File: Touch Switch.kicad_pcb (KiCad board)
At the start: 2 copper layers, 39 parts, among them J1 Conn_01x03_Pin, J2 Conn_02x04_Counter_Clockwise, K1 Relay_SPST-NO, K2 Relay_SPST-NO, K3 Relay_SPST-NO, K4 Relay_SPST-NO, Q1 MMBT3904, Q2 MMBT3904, Q3 MMBT3904, Q5 MMBT3904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

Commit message: PCB V1
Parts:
- removed the R13 at (47.0, 65.4)
- removed the R13 at (47.0, 31.2)
- removed S7133S1: ~, Package_SO:SOP-8_3.9x4.9mm_P1.27mm
- added C1: 2,2µF - 400V, Capacitor_THT:CP_Radial_D8.0mm_P3.50mm, F.Cu at (171.2, 98.8)
- added C2: 470µF - 10V, Capacitor_THT:CP_Radial_D6.3mm_P2.50mm, F.Cu at (190.8, 76.5)
- added C3: 330µF - 10V, Capacitor_THT:CP_Radial_D6.3mm_P2.50mm, F.Cu at (172.8, 71.1)
- added C4: 100nF - 10V, Capacitor_SMD:C_0805_2012Metric, F.Cu at (179.3, 66.1)
- added C5: 100pF - 400V, footprint:PFR5101J400J11L4BULK, F.Cu at (172.5, 106.0)
- added J3: Conn_01x01_Pin, Connector_PinHeader_2.54mm:PinHeader_1x01_P2.54mm_Vertical, F.Cu at (235.7, 92.4)
- added J4: Conn_01x01_Pin, Connector_PinHeader_2.54mm:PinHeader_1x01_P2.54mm_Vertical, F.Cu at (235.7, 79.1)
- added J5: Conn_01x01_Pin, Connector_PinHeader_2.54mm:PinHeader_1x01_P2.54mm_Vertical, F.Cu at (235.7, 105.6)
- added J6: Conn_01x01_Pin, Connector_PinHeader_2.54mm:PinHeader_1x01_P2.54mm_Vertical, F.Cu at (235.7, 65.9)
- added R11: 10K, Resistor_SMD:R_0805_2012Metric, F.Cu at (203.6, 92.2)
- added R13: 10K, Resistor_SMD:R_0805_2012Metric, F.Cu at (203.8, 66.0)
- added S713XS1: ~, Package_SO:SOP-8_3.9x4.9mm_P1.27mm, F.Cu at (161.4, 87.1)
- added T1: Transformer_1P_2S, footprint:transformer, F.Cu at (183.9, 90.9)
- J1: footprint Diode_SMD:D_SMA -> Connector_PinHeader_2.54mm:PinHeader_1x03_P2.54mm_Vertical
- moved K1 198.1 mm to (220.6, 95.7), turned to 0 degrees
- moved K4 188.4 mm to (220.6, 82.4), turned to 0 degrees
- moved K2 186.7 mm to (220.6, 108.9), turned to 0 degrees
- moved K3 183.5 mm to (220.6, 69.2), turned to 0 degrees
- moved D5 179.2 mm to (208.1, 98.0), turned to 90 degrees
- moved Q5 172.9 mm to (204.6, 96.2), turned to 0 degrees
- moved D7 168.8 mm to (208.1, 85.0), turned to 90 degrees
- moved D6 167.0 mm to (208.1, 111.5), turned to 90 degrees
- moved D8 163.5 mm to (208.1, 71.6), turned to 90 degrees
- moved Q3 163.2 mm to (204.6, 83.2), turned to 0 degrees
- moved Q1 161.8 mm to (204.8, 109.7), turned to 0 degrees
- moved R14 159.4 mm to (203.6, 78.5), turned to 90 degrees
- moved Q2 158.9 mm to (204.6, 70.0), turned to 0 degrees
- moved R12 158.4 mm to (203.8, 105.7), turned to 90 degrees
- moved J2 134.4 mm to (193.0, 86.9), turned to 90 degrees
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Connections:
- F1 pad 1: L -> L1
- J1 pad 1: L -> L1
- Q1 pad 1: CT3 -> CT4
- Q2 pad 1: CT4 -> CT3
- Q3 pad 1: CT2 -> CT1
- Q5 pad 1: CT1 -> CT2
- R12 pad 1: CT3 -> CT4
- R14 pad 1: CT2 -> CT1
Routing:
- net +5V: track 0.00 -> 171.9 mm
- net +3.3V: track 0.00 -> 60.0 mm, vias 0 -> 1
- net 310VDC: track 0.00 -> 51.2 mm
- net L: track 0.00 -> 48.0 mm
- net Prim: track 0.00 -> 31.0 mm
- net CT4: track 0.00 -> 27.3 mm
- net CT3: track 0.00 -> 25.5 mm
- net VCC_IC: track 0.00 -> 25.1 mm, vias 0 -> 2
- net Net-(C7-Pad1): track 0.00 -> 23.1 mm
- net Net-(D1-+): track 0.00 -> 17.5 mm
- net Net-(S713XS1-FB): track 0.00 -> 17.0 mm
- net Sec: track 0.00 -> 15.8 mm
- net N: track 0.00 -> 15.3 mm
- net CT2: track 0.00 -> 14.7 mm
- net Net-(D7-A): track 0.00 -> 11.1 mm
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- added copper zone on B.Cu, net GND
- added copper zone on F.Cu, net GND
- added copper zone on B.Cu, net GND2
- added copper zone on F.Cu, net GND2
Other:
- board outline added: 95 x 54 mm
- board text added: "Touch-Switch Power-Card"

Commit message: PCB V2
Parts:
- R5, R6: footprint Resistor_SMD:R_1206_3216Metric -> Resistor_SMD:R_0805_2012Metric
- moved F1 19.1 mm to (156.8, 64.5), turned to 180 degrees
- moved R11 13.8 mm to (193.2, 101.2), turned to -90 degrees
- moved D1 13.7 mm to (159.2, 79.0)
- moved J1 13.7 mm to (153.6, 75.8)
- moved C7 13.2 mm to (158.8, 69.0), turned to 0 degrees
- moved D7 10.7 mm to (199.0, 79.4)
- moved D6 9.88 mm to (198.2, 111.0)
- moved D8 9.88 mm to (198.2, 71.2)
- moved J3 9.88 mm to (225.8, 91.9)
- moved J4 9.88 mm to (225.8, 78.7)
- moved J5 9.88 mm to (225.8, 105.2)
- moved J6 9.88 mm to (225.8, 65.4)
- moved K1 9.88 mm to (210.8, 95.2)
- moved K2 9.88 mm to (210.8, 108.5)
- moved K3 9.88 mm to (210.8, 68.8)
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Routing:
- net +5V: track 171.9 -> 149.1 mm
- net Net-(D1-+): track 17.5 -> 37.6 mm
- net +3.3V: track 60.0 -> 43.3 mm
- net Net-(C7-Pad1): track 23.1 -> 13.5 mm
- net CT4: track 27.3 -> 18.3 mm
- net L1: track 4.63 -> 13.4 mm
- net N: track 15.3 -> 23.6 mm
- net CT1: track 12.5 -> 16.1 mm
- net Aux: track 10.9 -> 14.4 mm
- net CT3: track 25.5 -> 28.2 mm
- net R4: track 9.89 -> 7.34 mm
- net R3: track 9.89 -> 7.34 mm
- net R2: track 9.89 -> 7.34 mm
- net R1: track 9.89 -> 7.34 mm
- net Net-(D7-A): track 11.1 -> 8.84 mm
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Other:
- board size 95 x 54 mm -> 78 x 54 mm

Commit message: End 20-05-2024
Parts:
- added H1: MountingHole, MountingHole:MountingHole_2.2mm_M2_Pad_Via, F.Cu at (223.8, 71.9)
- added H2: MountingHole, MountingHole:MountingHole_2.2mm_M2_Pad_Via, F.Cu at (186.3, 68.4)
- added H3: MountingHole, MountingHole:MountingHole_2.2mm_M2_Pad_Via, F.Cu at (223.4, 111.0)
- added H4: MountingHole, MountingHole:MountingHole_2.2mm_M2_Pad_Via, F.Cu at (156.0, 111.0)

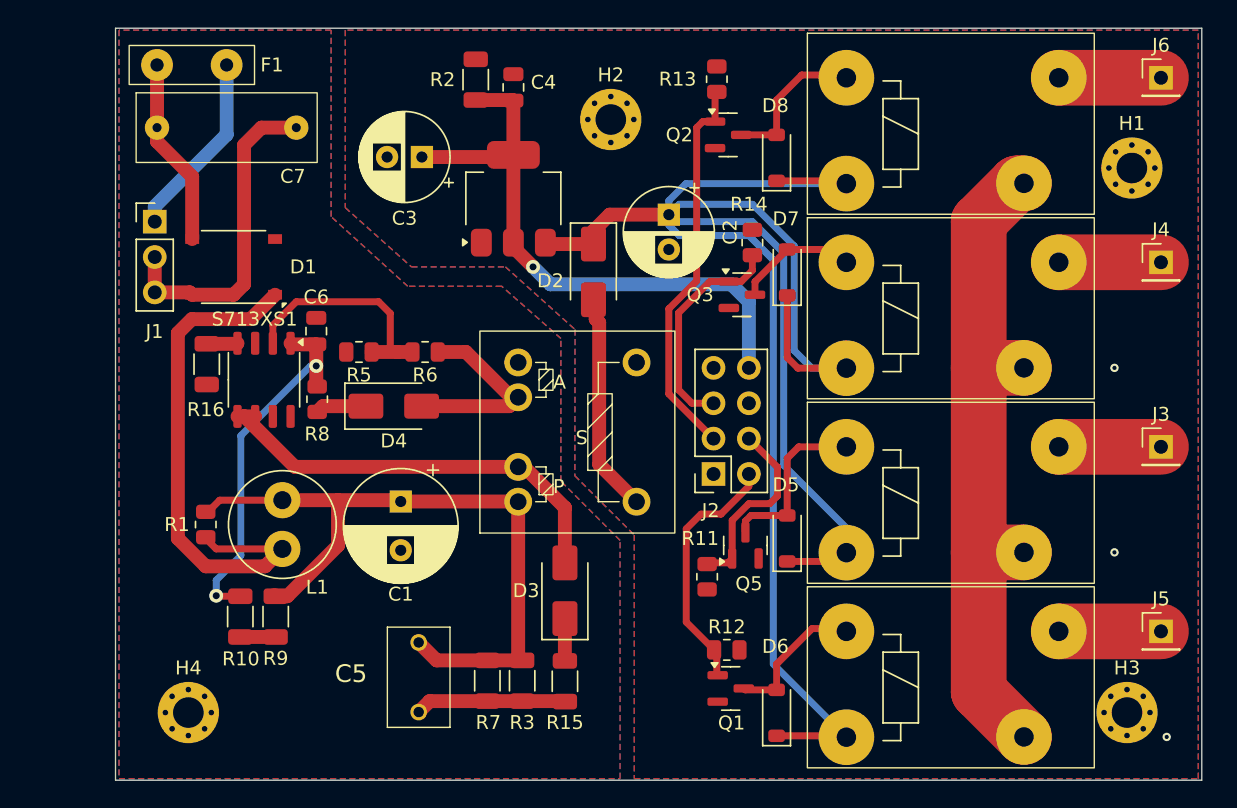
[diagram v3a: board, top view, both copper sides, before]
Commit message: Secondary without GND PLANE
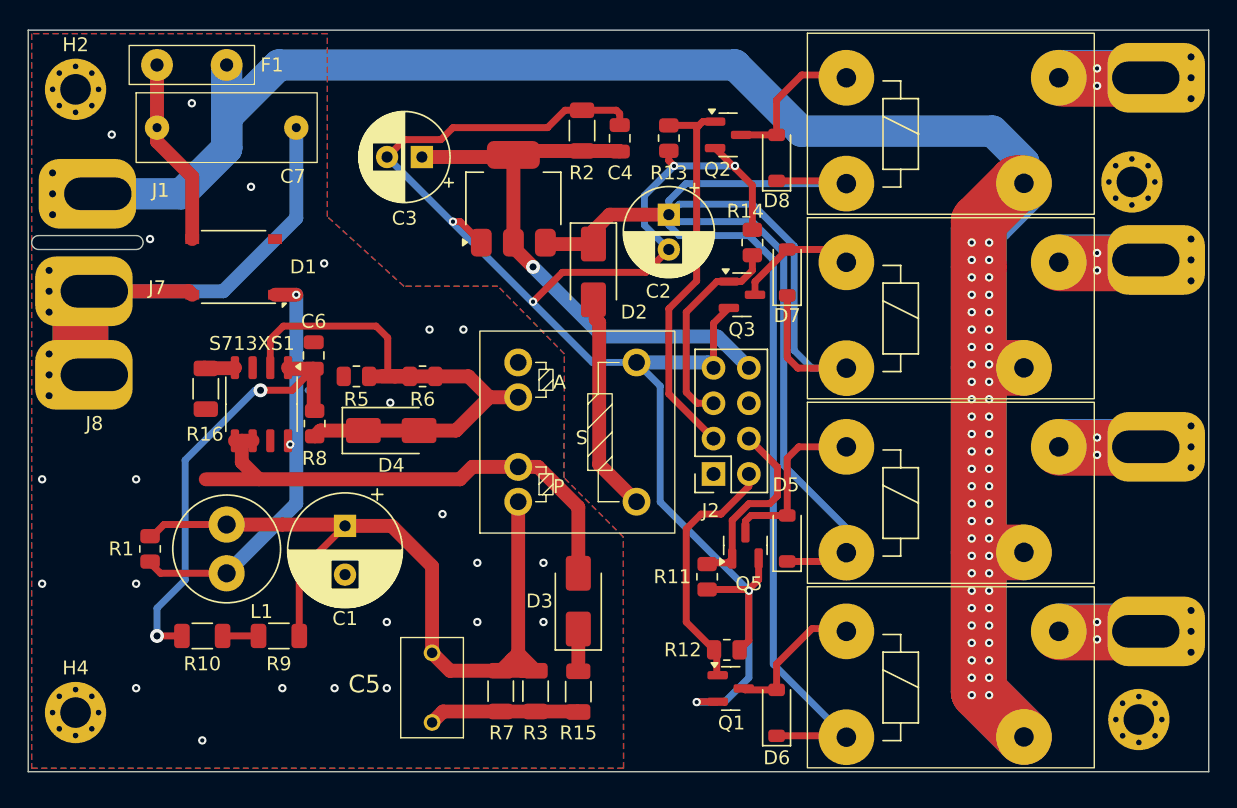
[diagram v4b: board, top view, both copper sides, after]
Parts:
- added J7: Conn_01x01_Pin, footprint:power_connector, F.Cu at (149.2, 80.8)
- added J8: Conn_01x01_Pin, footprint:power_connector, F.Cu at (149.2, 86.8)
- J1: value Conn_01x03_Pin -> Conn_01x01_Pin; footprint Connector_PinHeader_2.54mm:PinHeader_1x03_P2.54mm_Vertical -> footprint:power_connector
- J3, J4, J5, J6: footprint Connector_PinHeader_2.54mm:PinHeader_1x01_P2.54mm_Vertical -> footprint:power_connector
- moved H2 38.5 mm to (147.9, 66.2)
- moved C4 8.47 mm to (187.0, 69.8)
- moved R2 8.47 mm to (184.3, 69.2)
- moved H4 8.10 mm to (147.9, 111.0)
- moved R13 5.46 mm to (190.5, 69.8), turned to -90 degrees
- moved J1 4.55 mm to (149.5, 73.8), turned to -90 degrees
- moved C1 4.37 mm to (167.2, 97.6)
- moved L1 4.37 mm to (158.8, 101.0)
- moved R1 4.37 mm to (153.2, 99.2)
- moved R10 3.06 mm to (157.0, 105.5), turned to 180 degrees
- moved R16 1.77 mm to (157.2, 87.8)
- moved C6 1.76 mm to (165.0, 85.4)
- moved D4 1.76 mm to (170.6, 90.8)
- moved R5 1.76 mm to (168.1, 86.9)
- moved R6 1.76 mm to (172.8, 86.9)
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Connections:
- F1 pad 1: L1 -> (no net)
- J1 pad 1: L1 -> (no net)
- J3 pad 1: R1 -> (no net)
- J4 pad 1: R2 -> (no net)
- J5 pad 1: R3 -> (no net)
- J6 pad 1: R4 -> (no net)
- K1 pad 13: L -> (no net)
- K1 pad 14: R1 -> (no net)
- K2 pad 13: L -> (no net)
- K2 pad 14: R3 -> (no net)
- K3 pad 13: L -> (no net)
- K3 pad 14: R4 -> (no net)
- K4 pad 13: L -> (no net)
- K4 pad 14: R2 -> (no net)
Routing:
- net GND2: track 0.00 -> 129.7 mm, vias 3 -> 6
- net L: track 49.2 -> 174.7 mm, vias 0 -> 54
- net N: track 23.6 -> 44.3 mm
- net L1: track 13.4 -> 0.00 mm
- net 310VDC: track 52.2 -> 60.9 mm
- net Net-(D1-+): track 37.6 -> 29.5 mm, vias 0 -> 1
- net R4: track 7.34 -> 14.7 mm, vias 0 -> 2
- net R3: track 7.34 -> 14.7 mm, vias 0 -> 2
- net R1: track 7.34 -> 14.7 mm, vias 0 -> 2
- net R2: track 7.34 -> 14.6 mm, vias 0 -> 2
- net Prim: track 31.0 -> 37.6 mm
- net Aux: track 14.4 -> 20.2 mm
- net VCC_IC: track 26.0 -> 31.8 mm
- net +3.3V: track 43.3 -> 41.5 mm
- net CT1: track 16.1 -> 15.1 mm
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- removed copper zone on B.Cu, net GND2
- removed copper zone on F.Cu, net GND2
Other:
- board size 78 x 54 mm -> 84.8 x 53.2 mm

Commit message: PCB V2
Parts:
- removed D1: D_Bridge_+-AA, Diode_SMD:Diode_Bridge_Diotec_ABS
- removed H1, H2, H3, H4: MountingHole, MountingHole:MountingHole_2.2mm_M2_Pad_Via
- added D9: DF08M, Diode_SMD:Diode_Bridge_Diotec_ABS, F.Cu at (162.0, 94.8)
- C5: footprint footprint:PFR5101J400J11L4BULK -> Capacitor_SMD:C_1206_3216Metric
- moved J6 58.5 mm to (184.9, 108.3), turned to 0 degrees
- moved J1 43.7 mm to (176.2, 108.2), turned to 0 degrees
- moved J2 39.6 mm to (225.5, 70.3), turned to -90 degrees
- moved K3 36.7 mm to (181.7, 91.2), turned to -90 degrees
- moved F1 35.6 mm to (170.1, 97.5)
- moved R11 34.3 mm to (219.2, 78.8)
- moved D5 33.9 mm to (225.9, 77.9)
- moved Q5 33.2 mm to (222.4, 78.8), turned to 0 degrees
- moved D6 32.5 mm to (199.1, 78.5)
- moved C7 32.4 mm to (158.2, 101.4), turned to 180 degrees
- moved J4 32.3 mm to (212.3, 108.2), turned to 0 degrees
- moved Q1 30.7 mm to (195.4, 78.6)
- moved R10 29.8 mm to (149.0, 76.8), turned to 90 degrees
- moved R15 29.4 mm to (168.5, 84.5), turned to -90 degrees
- moved D3 29.4 mm to (162.5, 83.0), turned to 180 degrees
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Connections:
- F1 pad 1: (no net) -> L
- J1 pad 1: (no net) -> L
- J3 pad 1: (no net) -> R1
- J4 pad 1: (no net) -> R2
- J5 pad 1: (no net) -> R3
- J6 pad 1: (no net) -> R4
- K1 pad 13: (no net) -> L
- K1 pad 14: (no net) -> R1
- K2 pad 13: (no net) -> L
- K2 pad 14: (no net) -> R3
- K3 pad 13: (no net) -> L
- K3 pad 14: (no net) -> R4
- K4 pad 13: (no net) -> L
- K4 pad 14: (no net) -> R2
- Q1 pad 1: CT4 -> CT3
- Q2 pad 1: CT3 -> CT1
- Q3 pad 1: CT1 -> CT4
- R12 pad 1: CT4 -> CT3
- R13 pad 1: CT3 -> CT1
- R14 pad 1: CT1 -> CT4
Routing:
- net GND: track 0.00 -> 59.6 mm, vias 24 -> 3
- net L: track 174.7 -> 125.7 mm, vias 54 -> 46
- net CT1: track 15.1 -> 46.4 mm
- net GND2: track 129.7 -> 103.0 mm, vias 6 -> 4
- net VCC_IC: track 31.8 -> 8.73 mm, vias 2 -> 0
- net N: track 44.3 -> 23.2 mm, vias 0 -> 4
- net Prim: track 37.6 -> 16.8 mm
- net Net-(D9-+): track 29.5 -> 14.6 mm, vias 1 -> 0
- net +5V: track 149.1 -> 162.6 mm
- net +3.3V: track 41.5 -> 28.5 mm, vias 1 -> 0
- net CT4: track 18.3 -> 29.2 mm
- net Sec: track 15.8 -> 4.98 mm
- net CT2: track 13.9 -> 23.8 mm
- net R2: track 14.6 -> 23.8 mm, vias 2 -> 6
- net R3: track 14.7 -> 23.8 mm, vias 2 -> 6
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- removed copper zone on B.Cu, net GND
- removed copper zone on F.Cu, net GND
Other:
- board size 84.8 x 53.2 mm -> 82.9 x 49.8 mm

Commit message: PCB V3
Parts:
- moved R7 8.23 mm to (169.7, 91.8), turned to 0 degrees
- moved R3 4.97 mm to (169.7, 89.3), turned to 0 degrees
- moved F1 3.90 mm to (170.0, 101.4)
- moved C5 1.30 mm to (169.7, 86.8), turned to 0 degrees
- moved R15 1.17 mm to (169.7, 84.4), turned to 180 degrees
- moved D6 0.70 mm to (199.1, 77.8)
- moved C1 0.56 mm to (155.4, 85.5)
- moved D7 0.35 mm to (212.7, 78.2)
- moved T1 0.15 mm to (166.1, 72.9)
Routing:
- net +5V: track 162.6 -> 168.0 mm
- net Net-(C5-Pad2): track 12.6 -> 7.42 mm, vias 2 -> 0
- net 310VDC: track 56.8 -> 53.9 mm
- net Net-(C7-Pad1): track 10.6 -> 7.92 mm
- net L: track 125.7 -> 126.7 mm
- net Net-(D6-A): track 12.9 -> 13.5 mm
- net Prim: track 16.8 -> 16.7 mm, vias 0 -> 3
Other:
- outline, holes or cut-outs redrawn
